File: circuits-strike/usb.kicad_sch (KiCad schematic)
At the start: 14 parts, among them J2 USB_B_Micro, Q1 Crystal_12Mhz, Q2 Q_SS8050, Q3 Q_SS8550, U2 CH340T(SSOP20W)

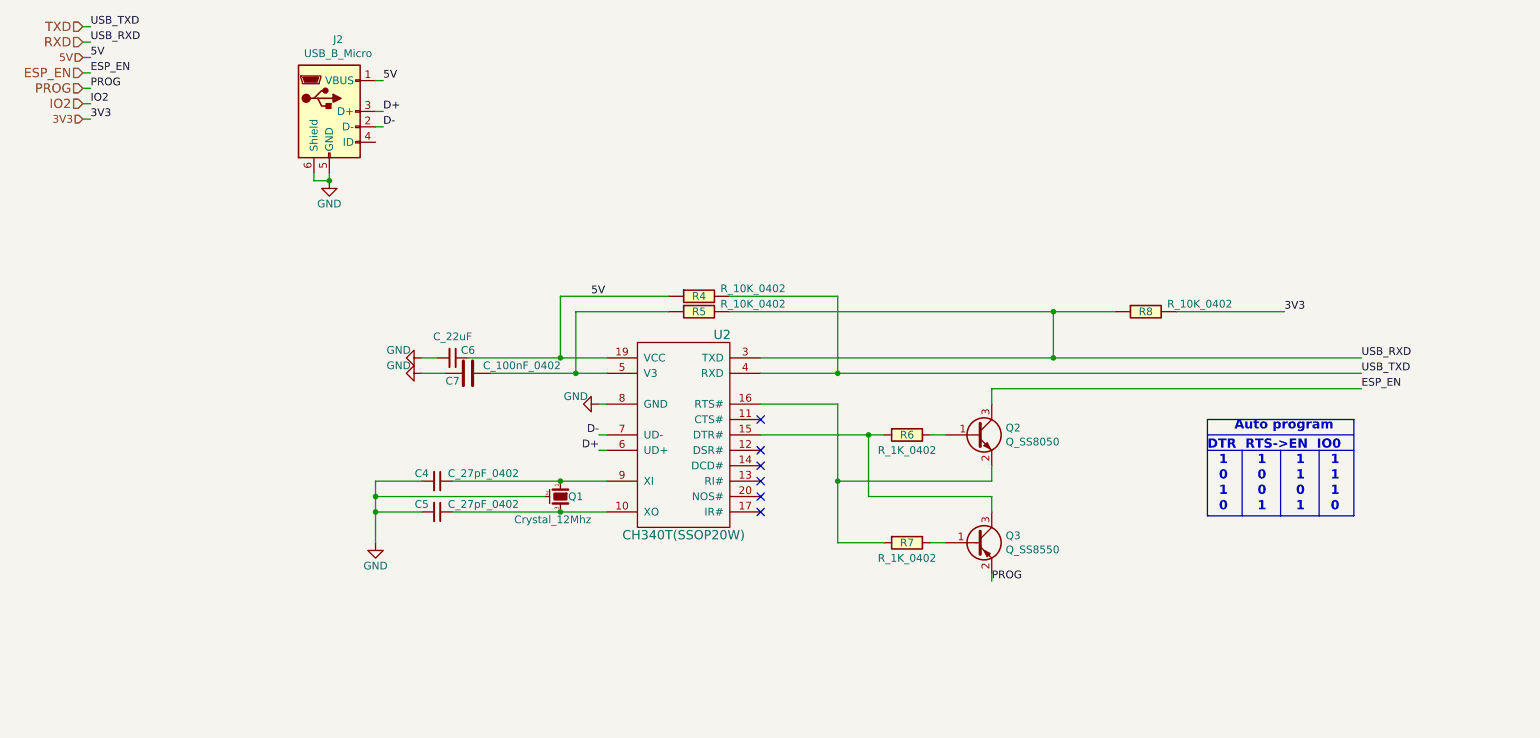
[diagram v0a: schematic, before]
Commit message: Finished schematic for shrinking PCB for residential systems
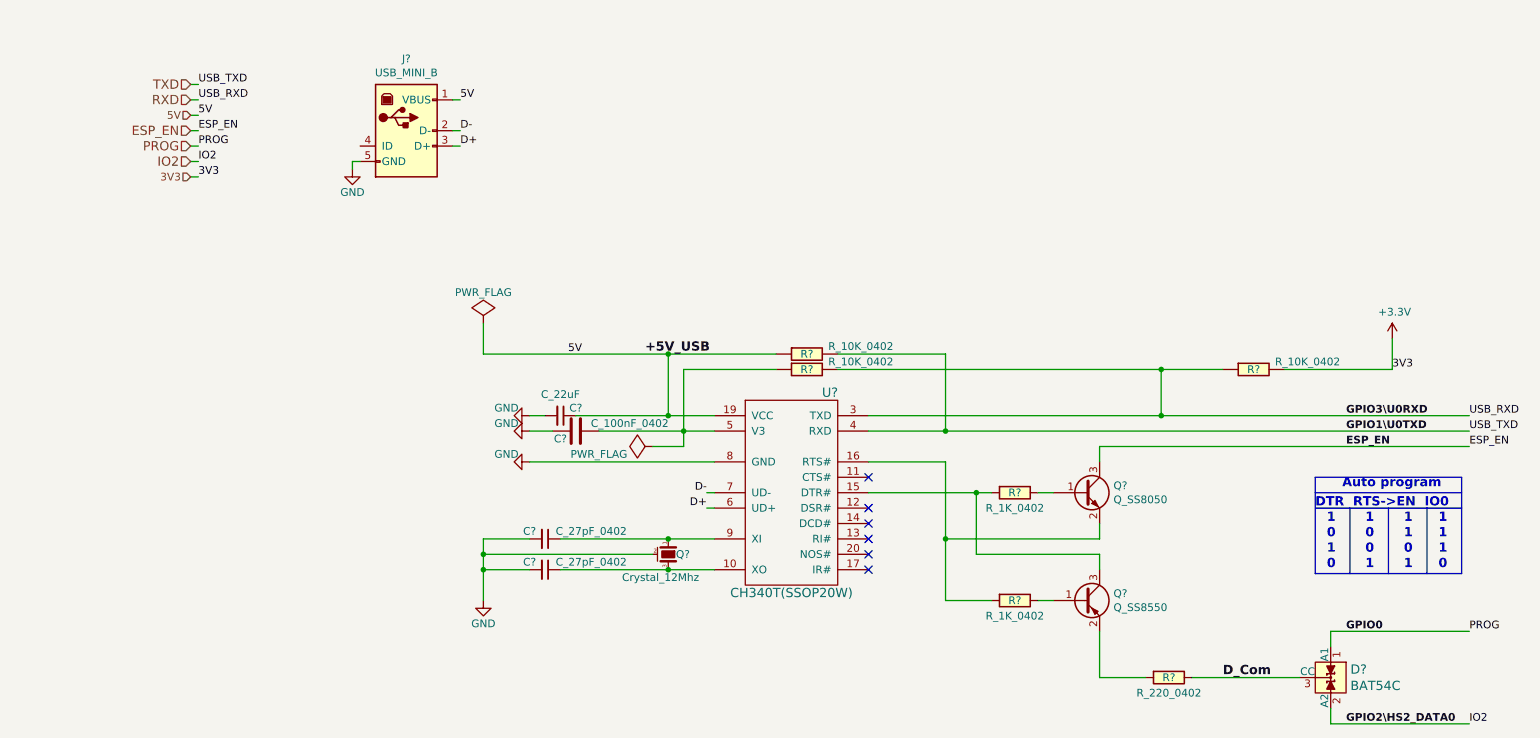
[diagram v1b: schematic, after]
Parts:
- removed C4, C5: C_27pF_0402, Capacitor_SMD:C_0402_1005Metric_Pad0.74x0.62mm_HandSolder, symbol Open_Automation:C_27pF_0402
- removed C6: C_22uF, Capacitor_SMD:C_0603_1608Metric_Pad1.08x0.95mm_HandSolder, symbol Open_Automation:C_22uF
- removed C7: C_100nF_0402, Capacitor_SMD:C_0402_1005Metric_Pad0.74x0.62mm_HandSolder, symbol Open_Automation:C_100nF_0402
- removed J2: USB_B_Micro, Connector_USB:USB_Micro-B_Amphenol_10118194_Horizontal, symbol strike-controller-rescue:USB_B_Micro-Open_Automation
- removed Q1: Crystal_12Mhz, Crystal:Crystal_SMD_3225-4Pin_3.2x2.5mm_HandSoldering, symbol Open_Automation:Crystal_12Mhz
- removed Q2: Q_SS8050, Package_TO_SOT_SMD:SOT-23, symbol Open_Automation:Q_SS8050
- removed Q3: Q_SS8550, Package_TO_SOT_SMD:SOT-23, symbol Open_Automation:Q_SS8550
- removed R4, R5, R8: R_10K_0402, Resistor_SMD:R_0402_1005Metric_Pad0.72x0.64mm_HandSolder, symbol Open_Automation:R_10K_0402
- removed R6, R7: R_1K_0402, Resistor_SMD:R_0402_1005Metric_Pad0.72x0.64mm_HandSolder, symbol Open_Automation:R_1K_0402
- removed U2: CH340T(SSOP20W), Open_Automation:SSOP-20W, symbol Open_Automation:CH340T(SSOP20W)
- added C?: C_100nF_0402, Capacitor_SMD:C_0402_1005Metric_Pad0.74x0.62mm_HandSolder, symbol Open_Automation:C_100nF_0402
- added C?: C_22uF, Capacitor_SMD:C_0603_1608Metric_Pad1.08x0.95mm_HandSolder, symbol Open_Automation:C_22uF
- added C? (x2): C_27pF_0402, Capacitor_SMD:C_0402_1005Metric_Pad0.74x0.62mm_HandSolder, symbol Open_Automation:C_27pF_0402
- added D?: BAT54C, Package_TO_SOT_SMD:SOT-23, symbol Open_Automation:BAT54C
- added J?: USB_MINI_B, Open_Automation:USB-mini-B-0548190519, symbol Open_Automation:USB_MINI_B
- added Q?: Q_SS8050, Package_TO_SOT_SMD:SOT-23, symbol Open_Automation:Q_SS8050
- added Q?: Q_SS8550, Package_TO_SOT_SMD:SOT-23, symbol Open_Automation:Q_SS8550
- added Q?: Crystal_12Mhz, Crystal:Crystal_SMD_3225-4Pin_3.2x2.5mm_HandSoldering, symbol Open_Automation:Crystal_12Mhz
- added R? (x3): R_10K_0402, Resistor_SMD:R_0402_1005Metric_Pad0.72x0.64mm_HandSolder, symbol Open_Automation:R_10K_0402
- added R? (x2): R_1K_0402, Resistor_SMD:R_0402_1005Metric_Pad0.72x0.64mm_HandSolder, symbol Open_Automation:R_1K_0402
- added R?: R_220_0402, Resistor_SMD:R_0402_1005Metric_Pad0.72x0.64mm_HandSolder, symbol Open_Automation:R_220_0402
- added U?: CH340T(SSOP20W), Open_Automation:SSOP-20W, symbol Open_Automation:CH340T(SSOP20W)
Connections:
- net 5V: now also C?.1, J?.1 (VBUS), R?.1, U?.19 (VCC)
- net D+: now also J?.3 (D+), U?.6 (UD+)
- net D-: now also J?.2 (D-), U?.7 (UD-)
- net ESP_EN: now also Q?.3 (C)
- net GND: now also C?.2, C?.2, C?.2, C?.2, J?.5 (GND), Q?.2 (case), Q?.4 (case), U?.8 (GND)
- net IO2: now also D?.2 (A2)
- net PROG: now also D?.1 (A1)
- net RXD: now also R?.1, R?.2, U?.3 (TXD)
- net TXD: now also R?.2, U?.4 (RXD)
- new net: Q?.1 (B), R?.1 (x2)
- new net: Q?.3 (C), R?.2, U?.15 (DTR#)
- new net: C?.1, R?.1, U?.5 (V3)
- new net: C?.1, Q?.3, U?.10 (XO)
- new net: Q?.2 (E), R?.2, U?.16 (RTS#)
- new net: C?.1, Q?.1, U?.9 (XI)
- new net: Q?.2 (E), R?.2
- new net +3V3: R?.2
- new net D_Com: D?.3 (CC), R?.1
